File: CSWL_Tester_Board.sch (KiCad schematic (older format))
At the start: 114 parts

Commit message: Ruan: add gpio list
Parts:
- added D1, D4: 1N5819HW-7-F, digikey-footprints:SOD-123, symbol dk_Diodes-Rectifiers-Single:1N5819HW-7-F
- added J11, J12, J13: Conn_01x02, symbol Connector_Generic:Conn_01x02
- added J14: Conn_01x04, RuanProject:Connector_Set_1x04_P2.54mm_Vertical, symbol Connector_Generic:Conn_01x04
- added J15: SPI1, symbol Connector_Generic:Conn_01x05
- added J16: Conn_02x10_Counter_Clockwise, symbol Connector_Generic:Conn_02x10_Counter_Clockwise
- added J17: Conn_01x02, RuanProject:KF129-2P, symbol Connector_Generic:Conn_01x02
- added K1, K4: G6SU-2, RuanProject:Relay_DPDT_Omron_G6SK-2, symbol Relay:G6SU-2
- added Q1, Q7: DMG2301L, Package_TO_SOT_SMD:SOT-23, symbol Transistor_FET:DMG2301L
- added Q10, Q4: 2N7002LT1G, digikey-footprints:SOT-23-3, symbol dk_Transistors-FETs-MOSFETs-Single:2N7002LT1G
- added R22, R23, R24, R31, R32, R33, R34, R35, R36, R37: 10K, Resistor_SMD:R_0603_1608Metric, symbol Device:R
- added R25, R26, R27: 0R, Resistor_SMD:R_0603_1608Metric, symbol Device:R
- added R38, R54: 33R, Resistor_SMD:R_0603_1608Metric, symbol Device:R
- added R40, R49, R57, R66: 100K, Resistor_SMD:R_0603_1608Metric, symbol Device:R
- added R44, R60: 330R (NC), Resistor_SMD:R_0603_1608Metric, symbol Device:R
- added R47, R63: 33R (NC), Resistor_SMD:R_0603_1608Metric, symbol Device:R
- added TP1, TP10, TP2, TP3, TP4, TP5, TP6, TP7, TP8, TP9: TestPoint, TestPoint:TestPoint_Loop_D2.50mm_Drill1.0mm, symbol Connector:TestPoint
- added U6, U9: EL817 (NC), digikey-footprints:SMD-4_4.6x7.62mm_P2.54mm, symbol Isolator:PC817
- gave numbers to parts that had none: 114
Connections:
- net labels added: CSWL_IN+, CSWL_IN-, CSWL_TO_Meter_EN, CSWL_VMeter+, CSWL_VMeter-, DC15V+, DC15V-, GPA0, GPA1, GPA4, GPA5, GPA6, GPA7, GPA8, I2C1_Alert, I2C1_SCL, I2C1_SDA, Meter_EN, Power_EN
- wire segments 375 -> 540
- no-connect marks 11 -> 15

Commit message: Ruan: fix
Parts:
- removed U10, U11, U6, U7, U8: EL817 (NC), digikey-footprints:SMD-4_4.6x7.62mm_P2.54mm, symbol Isolator:PC817
- added J?: Conn_01x02, RuanProject:KF129-2P, symbol Connector_Generic:Conn_01x02
- added U? (x5): EL817-S1-A (NC), digikey-footprints:SMD-4_4.6x7.62mm_P2.54mm, symbol Isolator:PC817
- K1, K2, K3, K4, K5, K6: value G6SU-2 -> G6SU-2 DC5
- U2: value STM32F103RCTx -> STM32F103RCT6
- U9: value EL817 (NC) -> EL817-S1-A (NC); alternative (none) -> Taiwan Semiconductor Corporation -- TPC817S1D RAG
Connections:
- net labels added: VMeter2+, VMeter2-
- wire segments 540 -> 547
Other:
- moved on the sheet: D4, J20, J21, K4, Q10, Q7, R53, R54, R57, R60, R63, R66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

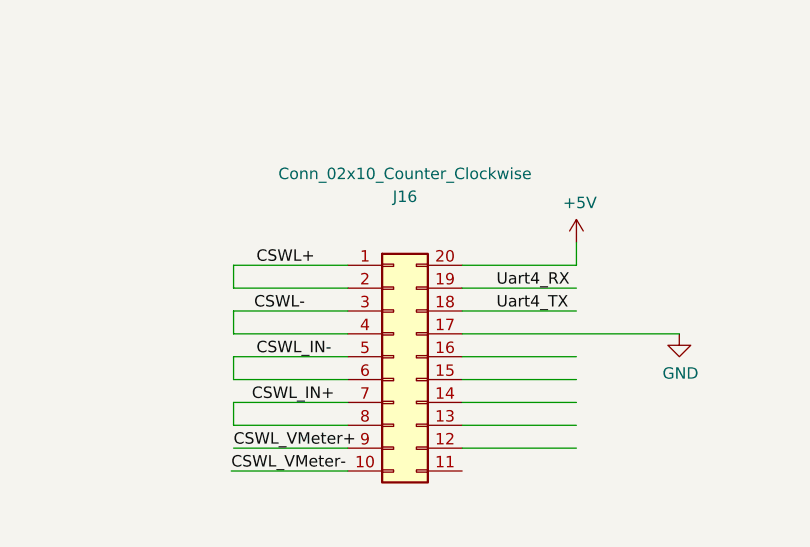
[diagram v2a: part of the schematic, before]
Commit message: Ruan: fix path
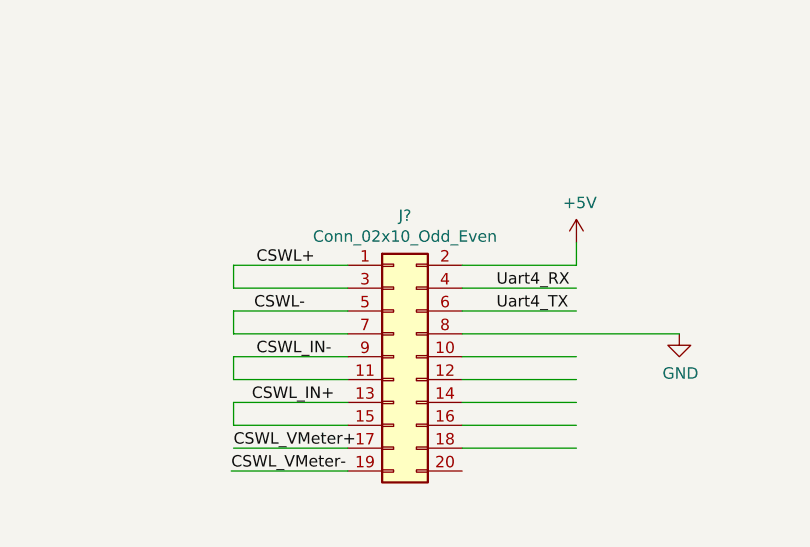
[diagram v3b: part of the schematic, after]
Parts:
- removed J16: Conn_02x10_Counter_Clockwise, symbol Connector_Generic:Conn_02x10_Counter_Clockwise
- added J?: Conn_02x10_Odd_Even, Connector_IDC:IDC-Header_2x10_P2.54mm_Vertical, symbol Connector_Generic:Conn_02x10_Odd_Even
- D1: Alternative (none) -> jcet B5819W; Category Discrete Semiconductor Products -> (none); DK_Datasheet_Link https://www.diodes.com/assets/Datasheets/ds30217.pdf -> (none); DK_Detail_Page /product-detail/en/diodes-incorporated/1N5819HW-7-F/1N5819H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 -> (none); Description DIODE SCHOTTKY 40V 1A SOD123 -> (none); Digi-Key_PN 1N5819HW-FDICT-ND -> (none); Family Diodes - Rectifiers - Single -> (none); MPN 1N5819HW-7-F -> (none); Manufacturer Diodes Incorporated -> (none); Status Active -> (none)
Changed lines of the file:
@@
 F 2 "digikey-footprints:SOD-123" H 16000 9300 60  0001 L CNN
 F 3 "https://www.diodes.com/assets/Datasheets/ds30217.pdf" H 16000 9400 60  0001 L CNN
-F 4 "1N5819HW-FDICT-ND" H 16000 9500 60  0001 L CNN "Digi-Key_PN"
-F 5 "1N5819HW-7-F" H 16000 9600 60  0001 L CNN "MPN"
-F 6 "Discrete Semiconductor Products" H 16000 9700 60  0001 L CNN "Category"
-F 7 "Diodes - Rectifiers - Single" H 16000 9800 60  0001 L CNN "Family"
-F 8 "https://www.diodes.com/assets/Datasheets/ds30217.pdf" H 16000 9900 60  0001 L CNN "DK_Datasheet_Link"
-F 9 "/product-detail/en/diodes-incorporated/1N5819HW-7-F/1N5819HW-FDICT-ND/815283" H 16000 10000 60  0001 L CNN "DK_Detail_Page"
-F 10 "DIODE SCHOTTKY 40V 1A SOD123" H 16000 10100 60  0001 L CNN "Description"
-F 11 "Diodes Incorporated" H 16000 10200 60  0001 L CNN "Manufacturer"
-F 12 "Active" H 16000 10300 60  0001 L CNN "Status"
+F 4 "jcet  B5819W " V 15800 9100 50  0001 C CNN "Alternative"
 	1    15800 9100
 	0    1    1    0
@@
 Text Label 17050 9650 0    50   ~ 0
 CSWL_IN-
-$Comp
-L Connector_Generic:Conn_02x10_Counter_Clockwise J16
-U 1 1 5D29A0A0
-P 15850 13300
-F 0 "J16" H 15900 14000 50  0000 C CNN
-F 1 "Conn_02x10_Counter_Clockwise" H 15900 14100 50  0000 C CNN
-F 2 "" H 15850 13300 50  0001 C CNN
-F 3 "~" H 15850 13300 50  0001 C CNN
-	1    15850 13300
-	1    0    0    -1
-$EndComp
 Wire Wire Line
 	15150 12900 15650 12900
@@
 Wire Wire Line
 	21860 7820 22010 7820
+$Comp
+L Connector_Generic:Conn_02x10_Odd_Even J?
+U 1 1 5D325CE2
+P 15850 13300
+F 0 "J?" H 15900 13917 50  0000 C CNN
+F 1 "Conn_02x10_Odd_Even" H 15900 13826 50  0000 C CNN
+F 2 "Connector_IDC:IDC-Header_2x10_P2.54mm_Vertical" H 15850 13300 50  0001 C CNN
+F 3 "~" H 15850 13300 50  0001 C CNN
+	1    15850 13300
+	1    0    0    -1
+$EndComp
 $EndSCHEMATC

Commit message: Ruan： start PCB
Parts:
- removed D6: 1N5819HW-7-F, digikey-footprints:SOD-123, symbol dk_Diodes-Rectifiers-Single:1N5819HW-7-F
- removed J23: Conn_01x02, RuanProject:KF129-2P, symbol Connector_Generic:Conn_01x02
- removed K6: G6SU-2 DC5, RuanProject:Relay_DPDT_Omron_G6SK-2, symbol Relay:G6SU-2
- removed Q12: 2N7002LT1G, digikey-footprints:SOT-23-3, symbol dk_Transistors-FETs-MOSFETs-Single:2N7002LT1G
- removed Q9: DMG2301L, Package_TO_SOT_SMD:SOT-23, symbol Transistor_FET:DMG2301L
- removed R56: 33R, Resistor_SMD:R_0603_1608Metric, symbol Device:R
- removed R59, R68: 100K, Resistor_SMD:R_0603_1608Metric, symbol Device:R
- removed R62: 330R (NC), Resistor_SMD:R_0603_1608Metric, symbol Device:R
- removed R65: 33R (NC), Resistor_SMD:R_0603_1608Metric, symbol Device:R
- removed U?: EL817-S1-A (NC), digikey-footprints:SMD-4_4.6x7.62mm_P2.54mm, symbol Isolator:PC817
- J11, J12, J13: footprint (none) -> RuanProject:Connector_Set_1x02_P2.54mm_Vertical
- J15: footprint (none) -> Connector_PinHeader_2.54mm:PinHeader_1x05_P2.54mm_Vertical
- gave numbers to parts that had none: 6
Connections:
- net labels added: LEDB_GB10, LEDB_GB11, LEDB_GB12, LEDB_GB13, LEDB_GB14, LEDB_GB9
- net labels removed: Dongle+, Dongle-
- wire segments 547 -> 509
- no-connect marks 15 -> 13
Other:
- moved on the sheet: D4, J16, J20, J21, J24, K4, Q10, Q7, R53, R54, R57, R60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

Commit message: Ruan: board PCB start
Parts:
- removed J21: Conn_01x02, RuanProject:KF129-2P, symbol Connector_Generic:Conn_01x02
- removed TP10, TP5, TP6, TP7, TP8, TP9: TestPoint, TestPoint:TestPoint_Loop_D2.50mm_Drill1.0mm, symbol Connector:TestPoint
- added J23: Conn_01x03, RuanProject:Connector_Set_1x03_P2.54mm_Vertical, symbol Connector_Generic:Conn_01x03
- added J25: USB_B_Micro, Connector_USB:USB_Micro-B_Molex-105017-0001, symbol Connector:USB_B_Micro
- added J26: Conn_01x04, Connector_PinHeader_2.00mm:PinHeader_1x04_P2.00mm_Vertical, symbol Connector_Generic:Conn_01x04
- added J27: Conn_01x10, Connector_PinHeader_2.54mm:PinHeader_1x10_P2.54mm_Vertical, symbol Connector_Generic:Conn_01x10
- added R56: 22R, Resistor_SMD:R_0603_1608Metric, symbol Device:R
- added R59: 10K, Resistor_SMD:R_0603_1608Metric, symbol Device:R
- added R62, R65, R68, R70, R71, R72, R73, R74, R75, R76, R77: 0R, Resistor_SMD:R_0603_1608Metric, symbol Device:R
- J10: footprint Connector_PinHeader_2.54mm:PinHeader_1x03_P2.54mm_Vertical -> Connector_PinSocket_2.54mm:PinSocket_1x03_P2.54mm_Vertical
- R53: value 0R -> 22R
- R69: footprint TestPoint:TestPoint_2Pads_Pitch5.08mm_Drill1.3mm -> Resistor_SMD:R_2512_6332Metric
- TP1, TP2, TP3, TP4: footprint TestPoint:TestPoint_Loop_D2.50mm_Drill1.0mm -> TestPoint:TestPoint_THTPad_2.0x2.0mm_Drill1.0mm
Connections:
- net labels added: GPA15, GPA4_SPI1_NSS, GPA5_SPI1_SCK, GPA6_SPI1_MISO, GPA7_SPI1_MOSI, GPB0, GPB1, GPB12, GPB13, GPB14, GPB15, GPB2, GPC0, GPC1, SWDCLK, SWDIO, USBDM, USBDP
- net labels removed: Dongle_EN, GPA4, GPA5, GPA6, GPA7, LEDB_GB13, LEDB_GB14, VMeter2+, VMeter2-
- wire segments 509 -> 593
- no-connect marks 13 -> 25
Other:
- moved on the sheet: J15, R69

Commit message: Ruan: pcb developing
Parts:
- removed R62, R68, R70, R71: 0R, Resistor_SMD:R_0603_1608Metric, symbol Device:R
- added J21, J28, J29, J30: Fix hole, RuanProject:Local_Hole_D5.0mm_Drill3.5mm, symbol Connector_Generic:Conn_01x01
- added J31: Conn_Coaxial_Power, Connector_BarrelJack:BarrelJack_Horizontal, symbol Connector:Conn_Coaxial_Power
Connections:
- wire segments 593 -> 591
- no-connect marks 25 -> 29
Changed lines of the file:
@@
 LEDB_GB12
-Wire Wire Line
-	16772 10302 16922 10302
-$Comp
-L power:GND #PWR?
-U 1 1 5D35CBAF
-P 16922 10302
-AR Path="/5D3C2445/5D35CBAF" Ref="#PWR?"  Part="1"
-AR Path="/5D3F6A12/5D35CBAF" Ref="#PWR?"  Part="1"
-AR Path="/5D3FDFBE/5D35CBAF" Ref="#PWR?"  Part="1"
-AR Path="/5D403D60/5D35CBAF" Ref="#PWR?"  Part="1"
-AR Path="/5D35CBAF" Ref="#PWR0101"  Part="1"
-F 0 "#PWR0101" H 16922 10052 50  0001 C CNN
-F 1 "GND" H 16927 10129 50  0000 C CNN
-F 2 "" H 16922 10302 50  0001 C CNN
-F 3 "" H 16922 10302 50  0001 C CNN
-	1    16922 10302
-	1    0    0    -1
-$EndComp
-Wire Wire Line
-	17166 6902 17316 6902
-$Comp
-L power:GND #PWR?
-U 1 1 5D42C86B
-P 17316 6902
-AR Path="/5D3C2445/5D42C86B" Ref="#PWR?"  Part="1"
-AR Path="/5D3F6A12/5D42C86B" Ref="#PWR?"  Part="1"
-AR Path="/5D3FDFBE/5D42C86B" Ref="#PWR?"  Part="1"
-AR Path="/5D403D60/5D42C86B" Ref="#PWR?"  Part="1"
-AR Path="/5D42C86B" Ref="#PWR0102"  Part="1"
-F 0 "#PWR0102" H 17316 6652 50  0001 C CNN
-F 1 "GND" H 17321 6729 50  0000 C CNN
-F 2 "" H 17316 6902 50  0001 C CNN
-F 3 "" H 17316 6902 50  0001 C CNN
-	1    17316 6902
-	1    0    0    -1
-$EndComp
-$Comp
-L Device:R R68
-U 1 1 5D42C871
-P 17016 6902
-AR Path="/5D42C871" Ref="R68"  Part="1"
-AR Path="/5D3C2445/5D42C871" Ref="R?"  Part="1"
-F 0 "R68" V 17066 6752 50  0000 R CNN
-F 1 "0R" V 17066 7152 50  0000 R CNN
-F 2 "Resistor_SMD:R_0603_1608Metric" V 16946 6902 50  0001 C CNN
-F 3 "~" H 17016 6902 50  0001 C CNN
-	1    17016 6902
-	0    -1   -1   0
-$EndComp
 Wire Wire Line
 	16650 6650 16650 6902
@@
 	16650 6902 16650 6950
 Wire Wire Line
-	21437 7021 21587 7021
-$Comp
-L power:GND #PWR?
-U 1 1 5D4FACF6
-P 21587 7021
-AR Path="/5D3C2445/5D4FACF6" Ref="#PWR?"  Part="1"
-AR Path="/5D3F6A12/5D4FACF6" Ref="#PWR?"  Part="1"
-AR Path="/5D3FDFBE/5D4FACF6" Ref="#PWR?"  Part="1"
-AR Path="/5D403D60/5D4FACF6" Ref="#PWR?"  Part="1"
-AR Path="/5D4FACF6" Ref="#PWR0103"  Part="1"
-F 0 "#PWR0103" H 21587 6771 50  0001 C CNN
-F 1 "GND" H 21592 6848 50  0000 C CNN
-F 2 "" H 21587 7021 50  0001 C CNN
-F 3 "" H 21587 7021 50  0001 C CNN
-	1    21587 7021
-	1    0    0    -1
-$EndComp
-$Comp
-L Device:R R71
-U 1 1 5D4FACFC
-P 21287 7021
-AR Path="/5D4FACFC" Ref="R71"  Part="1"
-AR Path="/5D3C2445/5D4FACFC" Ref="R?"  Part="1"
-F 0 "R71" V 21337 6871 50  0000 R CNN
-F 1 "0R" V 21337 7271 50  0000 R CNN
-F 2 "Resistor_SMD:R_0603_1608Metric" V 21217 7021 50  0001 C CNN
-F 3 "~" H 21287 7021 50  0001 C CNN
-	1    21287 7021
-	0    -1   -1   0
-$EndComp
-Wire Wire Line
 	21137 7021 21003 7021
-Wire Wire Line
-	21254 3761 21404 3761
-$Comp
-L power:GND #PWR?
-U 1 1 5D58640C
-P 21404 3761
-AR Path="/5D3C2445/5D58640C" Ref="#PWR?"  Part="1"
-AR Path="/5D3F6A12/5D58640C" Ref="#PWR?"  Part="1"
-AR Path="/5D3FDFBE/5D58640C" Ref="#PWR?"  Part="1"
-AR Path="/5D403D60/5D58640C" Ref="#PWR?"  Part="1"
-AR Path="/5D58640C" Ref="#PWR0104"  Part="1"
-F 0 "#PWR0104" H 21404 3511 50  0001 C CNN
-F 1 "GND" H 21409 3588 50  0000 C CNN
-F 2 "" H 21404 3761 50  0001 C CNN
-F 3 "" H 21404 3761 50  0001 C CNN
-	1    21404 3761
-	1    0    0    -1
-$EndComp
-$Comp
-L Device:R R70
-U 1 1 5D586412
-P 21104 3761
-AR Path="/5D586412" Ref="R70"  Part="1"
-AR Path="/5D3C2445/5D586412" Ref="R?"  Part="1"
-F 0 "R70" V 21154 3611 50  0000 R CNN
-F 1 "0R" V 21154 4011 50  0000 R CNN
-F 2 "Resistor_SMD:R_0603_1608Metric" V 21034 3761 50  0001 C CNN
-F 3 "~" H 21104 3761 50  0001 C CNN
-	1    21104 3761
-	0    -1   -1   0
-$EndComp
 Wire Wire Line
 	20954 3761 20751 3761
@@
 Wire Wire Line
 	16463 12404 16463 12403
-$Comp
-L Device:R R62
-U 1 1 5D35CBB5
-P 16622 10302
-AR Path="/5D35CBB5" Ref="R62"  Part="1"
-AR Path="/5D3C2445/5D35CBB5" Ref="R?"  Part="1"
-F 0 "R62" V 16672 10152 50  0000 R CNN
-F 1 "0R" V 16672 10552 50  0000 R CNN
-F 2 "Resistor_SMD:R_0603_1608Metric" V 16552 10302 50  0001 C CNN
-F 3 "~" H 16622 10302 50  0001 C CNN
-	1    16622 10302
-	0    -1   -1   0
-$EndComp
 Wire Wire Line
 	16472 10302 16250 10302
@@
 Text Label 9300 9900 0    50   ~ 0
 Vuart
+$Comp
+L Connector_Generic:Conn_01x01 J30
+U 1 1 5D3B5292
+P 18270 12020
+F 0 "J30" H 18350 12062 50  0000 L CNN
+F 1 "Fix hole" H 18350 11971 50  0000 L CNN
+F 2 "RuanProject:Local_Hole_D5.0mm_Drill3.5mm" H 18270 12020 50  0001 C CNN
+F 3 "~" H 18270 12020 50  0001 C CNN
+	1    18270 12020
+	1    0    0    -1
+$EndComp
+$Comp
+L Connector_Generic:Conn_01x01 J29
+U 1 1 5D3B8646
+P 18250 12254
+F 0 "J29" H 18330 12296 50  0000 L CNN
+F 1 "Fix hole" H 18330 12205 50  0000 L CNN
+F 2 "RuanProject:Local_Hole_D5.0mm_Drill3.5mm" H 18250 12254 50  0001 C CNN
+F 3 "~" H 18250 12254 50  0001 C CNN
+	1    18250 12254
+	1    0    0    -1
+$EndComp
+$Comp
+L Connector_Generic:Conn_01x01 J28
+U 1 1 5D3B88D3
+P 18245 12523
+F 0 "J28" H 18325 12565 50  0000 L CNN
+F 1 "Fix hole" H 18325 12474 50  0000 L CNN
+F 2 "RuanProject:Local_Hole_D5.0mm_Drill3.5mm" H 18245 12523 50  0001 C CNN
+F 3 "~" H 18245 12523 50  0001 C CNN
+	1    18245 12523
+	1    0    0    -1
+$EndComp
+$Comp
+L Connector_Generic:Conn_01x01 J21
+U 1 1 5D42F59E
+P 18239 12735
+F 0 "J21" H 18319 12777 50  0000 L CNN
+F 1 "Fix hole" H 18319 12686 50  0000 L CNN
+F 2 "RuanProject:Local_Hole_D5.0mm_Drill3.5mm" H 18239 12735 50  0001 C CNN
+F 3 "~" H 18239 12735 50  0001 C CNN
+	1    18239 12735
+	1    0    0    -1
+$EndComp
+NoConn ~ 18070 12020
+NoConn ~ 18050 12254
+NoConn ~ 18045 12523
+NoConn ~ 18039 12735
+$Comp
+L Connector:Conn_Coaxial_Power J31
+U 1 1 5D3D36E9
+P 20050 8325
+F 0 "J31" H 20138 8321 50  0000 L CNN
+F 1 "Conn_Coaxial_Power" H 20138 8230 50  0001 L CNN
+F 2 "Connector_BarrelJack:BarrelJack_Horizontal" H 20050 8275 50  0001 C CNN
+F 3 "~" H 20050 8275 50  0001 C CNN
+	1    20050 8325
+	1    0    0    -1
+$EndComp
+$Comp
+L power:+5VA #PWR021
+U 1 1 5D3D455F
+P 20050 8150
+F 0 "#PWR021" H 20050 8000 50  0001 C CNN
+F 1 "+5VA" H 20065 8323 50  0000 C CNN
+F 2 "" H 20050 8150 50  0001 C CNN
+F 3 "" H 20050 8150 50  0001 C CNN
+	1    20050 8150
+	1    0    0    -1
+$EndComp
+Wire Wire Line
+	20050 8150 20050 8225
+Wire Wire Line
+	20050 8525 20050 8675
+$Comp
+L power:GNDS #PWR036
+U 1 1 5D498121
+P 20050 8675
+F 0 "#PWR036" H 20050 8425 50  0001 C CNN
+F 1 "GNDS" H 20055 8502 50  0000 C CNN
+F 2 "" H 20050 8675 50  0001 C CNN
+F 3 "" H 20050 8675 50  0001 C CNN
+	1    20050 8675
+	1    0    0    -1
+$EndComp
 $EndSCHEMATC

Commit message: Ruan: base ok V0
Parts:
- added R62: 100K, Resistor_SMD:R_0603_1608Metric, symbol Device:R
- added R68, R70, R71: 0R, Resistor_SMD:R_0603_1608Metric, symbol Device:R
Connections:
- net labels added: GNDA1, GNDA2, GNDA3
- wire segments 591 -> 600
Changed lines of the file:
@@
 Wire Wire Line
 	15956 12304 16456 12304
-Text Label 15056 12104 0    50   ~ 0
+Text Label 15024 12304 0    50   ~ 0
 CSWL+
-Text Label 15046 12304 0    50   ~ 0
+Text Label 15001 12104 0    50   ~ 0
 CSWL-
 Text Label 16028 12304 0    50   ~ 0
@@
 	7000 4400 7000 4450
 $Comp
-L power:GND #PWR040
-U 1 1 5D7FDCB4
-P 7000 4500
-F 0 "#PWR040" H 7000 4250 50  0001 C CNN
-F 1 "GND" H 7005 4327 50  0000 C CNN
-F 2 "" H 7000 4500 50  0001 C CNN
-F 3 "" H 7000 4500 50  0001 C CNN
-	1    7000 4500
-	1    0    0    -1
-$EndComp
-$Comp
 L Device:R R22
 U 1 1 5D7C14A4
@@
 	7000 5300 7000 5350
 $Comp
-L power:GND #PWR041
-U 1 1 5D9A9CFB
-P 7000 5400
-F 0 "#PWR041" H 7000 5150 50  0001 C CNN
-F 1 "GND" H 7005 5227 50  0000 C CNN
-F 2 "" H 7000 5400 50  0001 C CNN
-F 3 "" H 7000 5400 50  0001 C CNN
-	1    7000 5400
-	1    0    0    -1
-$EndComp
-$Comp
 L Device:R R23
 U 1 1 5D9A9D05
@@
 	7000 6300 7000 6350
 $Comp
-L power:GND #PWR042
-U 1 1 5D9EB318
-P 7000 6400
-F 0 "#PWR042" H 7000 6150 50  0001 C CNN
-F 1 "GND" H 7005 6227 50  0000 C CNN
-F 2 "" H 7000 6400 50  0001 C CNN
-F 3 "" H 7000 6400 50  0001 C CNN
-	1    7000 6400
-	1    0    0    -1
-$EndComp
-$Comp
 L Device:R R24
 U 1 1 5D9EB322
@@
 Wire Wire Line
 	14956 12804 14956 12704
+Text Label 14946 13004 0    50   ~ 0
+CSWL_VMeter+
 Text Label 14956 12904 0    50   ~ 0
-CSWL_VMeter+
-Text Label 14946 13004 0    50   ~ 0
 CSWL_VMeter-
-Text Label 15036 12704 0    50   ~ 0
+Text Label 15000 12504 0    50   ~ 0
 CSWL_IN+
-Text Label 15056 12504 0    50   ~ 0
+Text Label 15000 12704 0    50   ~ 0
 CSWL_IN-
 Wire Wire Line
@@
 Text Label 7800 1700 0    50   ~ 0
 USBDM
-Text Label 9800 2500 0    50   ~ 0
+Text Label 9800 3300 0    50   ~ 0
 GPA8
 Text Label 4050 4650 0    50   ~ 0
 GPB2
+Text Label 9800 2500 0    50   ~ 0
+GPB1
 Text Label 9800 2600 0    50   ~ 0
-GPB1
-Text Label 9800 2700 0    50   ~ 0
 GPB2
 Text Label 4050 5650 0    50   ~ 0
@@
 Text Label 4050 5950 0    50   ~ 0
 GPB15
-Text Label 9800 2800 0    50   ~ 0
+Text Label 9800 2900 0    50   ~ 0
 GPB12
-Text Label 9800 2900 0    50   ~ 0
+Text Label 9800 3000 0    50   ~ 0
 GPB13
-Text Label 9800 3000 0    50   ~ 0
+Text Label 9800 3100 0    50   ~ 0
 GPB14
-Text Label 9800 3100 0    50   ~ 0
+Text Label 9800 3200 0    50   ~ 0
 GPB15
 Wire Wire Line
@@
 Text Label 2250 4550 2    50   ~ 0
 GPC1
-Text Label 9800 3200 0    50   ~ 0
+Text Label 9800 2800 0    50   ~ 0
 GPC0
-Text Label 9800 3300 0    50   ~ 0
+Text Label 9800 2700 0    50   ~ 0
 GPC1
 $Comp
@@
 $EndComp
 Wire Wire Line
-	20050 8150 20050 8225
-Wire Wire Line
 	20050 8525 20050 8675
 $Comp
@@
 	1    0    0    -1
 $EndComp
+$Comp
+L Device:R R62
+U 1 1 5D48ABA7
+P 20460 8212
+AR Path="/5D48ABA7" Ref="R62"  Part="1"
+AR Path="/5D3C2445/5D48ABA7" Ref="R?"  Part="1"
+F 0 "R62" H 20610 8162 50  0000 R CNN
+F 1 "100K" H 20710 8262 50  0000 R CNN
+F 2 "Resistor_SMD:R_0603_1608Metric" V 20390 8212 50  0001 C CNN
+F 3 "~" H 20460 8212 50  0001 C CNN
+	1    20460 8212
+	0    1    1    0
+$EndComp
+Wire Wire Line
+	20050 8150 20050 8212
+Connection ~ 20050 8212
+Wire Wire Line
+	20050 8212 20050 8225
+$Comp
+L power:+5V #PWR054
+U 1 1 5D4EAFBE
+P 20707 8212
+F 0 "#PWR054" H 20707 8062 50  0001 C CNN
+F 1 "+5V" H 20722 8385 50  0000 C CNN
+F 2 "" H 20707 8212 50  0001 C CNN
+F 3 "" H 20707 8212 50  0001 C CNN
+	1    20707 8212
+	1    0    0    -1
+$EndComp
+Wire Wire Line
+	20610 8212 20707 8212
+Wire Wire Line
+	20050 8212 20310 8212
+Text GLabel 7000 4500 0    50   Input ~ 0
+GNDA1
+Text GLabel 7000 5400 0    50   Input ~ 0
+GNDA2
+Text GLabel 7000 6400 0    50   Input ~ 0
+GNDA3
+$Comp
+L power:GND #PWR040
+U 1 1 5D4FB44A
+P 7336 4502
+F 0 "#PWR040" H 7336 4252 50  0001 C CNN
+F 1 "GND" H 7341 4329 50  0000 C CNN
+F 2 "" H 7336 4502 50  0001 C CNN
+F 3 "" H 7336 4502 50  0001 C CNN
+	1    7336 4502
+	1    0    0    -1
+$EndComp
+$Comp
+L Device:R R68
+U 1 1 5D5BA1CC
+P 7150 4500
+AR Path="/5D5BA1CC" Ref="R68"  Part="1"
+AR Path="/5D3C2445/5D5BA1CC" Ref="R?"  Part="1"
+F 0 "R68" V 7058 4607 50  0000 R CNN
+F 1 "0R" V 7053 4495 50  0000 R CNN
+F 2 "Resistor_SMD:R_0603_1608Metric" V 7080 4500 50  0001 C CNN
+F 3 "~" H 7150 4500 50  0001 C CNN
+	1    7150 4500
+	0    -1   -1   0
+$EndComp
+Wire Wire Line
+	7300 4500 7336 4500
+Wire Wire Line
+	7336 4500 7336 4502
+$Comp
+L power:GND #PWR041
+U 1 1 5D67AD33
+P 7336 5402
+F 0 "#PWR041" H 7336 5152 50  0001 C CNN
+F 1 "GND" H 7341 5229 50  0000 C CNN
+F 2 "" H 7336 5402 50  0001 C CNN
+F 3 "" H 7336 5402 50  0001 C CNN
+	1    7336 5402
+	1    0    0    -1
+$EndComp
+$Comp
+L Device:R R70
+U 1 1 5D67AD39
+P 7150 5400
+AR Path="/5D67AD39" Ref="R70"  Part="1"
+AR Path="/5D3C2445/5D67AD39" Ref="R?"  Part="1"
+F 0 "R70" V 7058 5507 50  0000 R CNN
+F 1 "0R" V 7053 5395 50  0000 R CNN
+F 2 "Resistor_SMD:R_0603_1608Metric" V 7080 5400 50  0001 C CNN
+F 3 "~" H 7150 5400 50  0001 C CNN
+	1    7150 5400
+	0    -1   -1   0
+$EndComp
+Wire Wire Line
+	7300 5400 7336 5400
+Wire Wire Line
+	7336 5400 7336 5402
+$Comp
+L power:GND #PWR042
+U 1 1 5D79B31D
+P 7336 6402
+F 0 "#PWR042" H 7336 6152 50  0001 C CNN
+F 1 "GND" H 7341 6229 50  0000 C CNN
+F 2 "" H 7336 6402 50  0001 C CNN
+F 3 "" H 7336 6402 50  0001 C CNN
+	1    7336 6402
+	1    0    0    -1
+$EndComp
+$Comp
+L Device:R R71
+U 1 1 5D79B323
+P 7150 6400
+AR Path="/5D79B323" Ref="R71"  Part="1"
+AR Path="/5D3C2445/5D79B323" Ref="R?"  Part="1"
+F 0 "R71" V 7058 6507 50  0000 R CNN
+F 1 "0R" V 7053 6395 50  0000 R CNN
+F 2 "Resistor_SMD:R_0603_1608Metric" V 7080 6400 50  0001 C CNN
+F 3 "~" H 7150 6400 50  0001 C CNN
+	1    7150 6400
+	0    -1   -1   0
+$EndComp
+Wire Wire Line
+	7300 6400 7336 6400
+Wire Wire Line
+	7336 6400 7336 6402
 $EndSCHEMATC
